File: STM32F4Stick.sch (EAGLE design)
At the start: 42 parts, among them U1 MIC5219 3.3V, U2 USD-SOCKETNEW

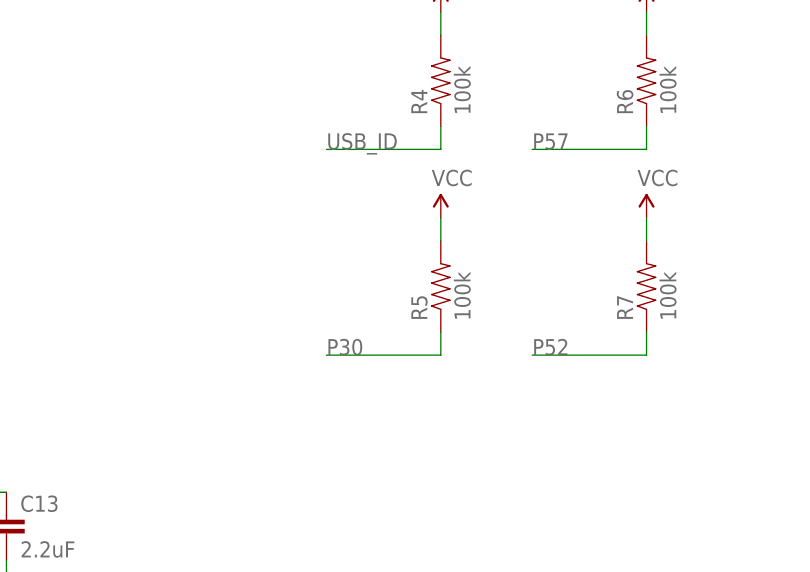
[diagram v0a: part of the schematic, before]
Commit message: Version 1 Rev B. Added STM32F401 support. Added Readme. Added image. Added libraries. Added BOM.
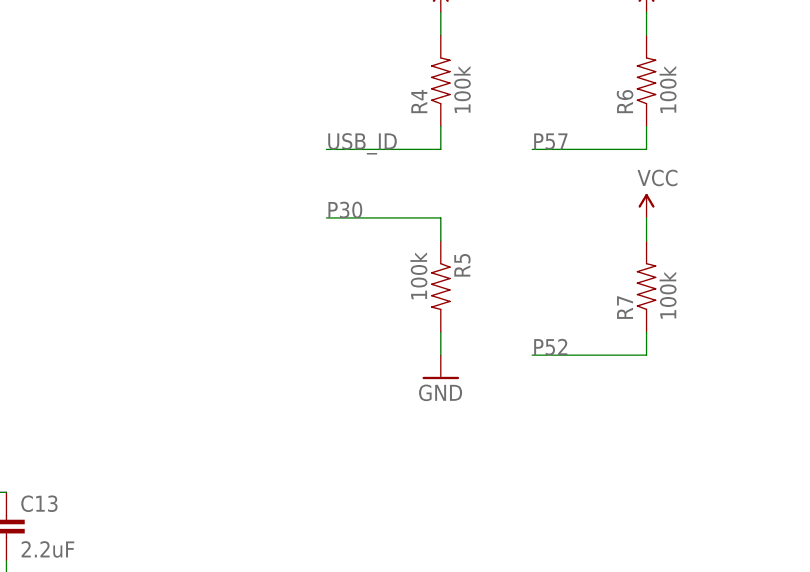
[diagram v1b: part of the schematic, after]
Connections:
- net GND: now also R5.2
- net VCC: no longer R5.2
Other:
- note added: "For STM32F401 support C13 should be 0 ohm resistor"
- note added: "For STM32F401 support C5 should be 0 ohm resistor"
- note added: "For STM32F401 support R5 should be 4.7uF Cap"
- note added: "PA10, PB5, PB11, PC11 needs stable levels for USB bootloader PA10 (USB_ID) is pulled high PB11 (P30) is pulled low PB5 (P57) is pulled high PC11 (P52) is pulled high"
- note removed: "PA10, PB5, PB11, PC11 needs stable levels for USB bootloader PA10 (USB_ID) is pulled high PB11 (P30) is pulled high PB5 (P57) is pulled high PC11 (P52) is pulled high"
- moved on the sheet: R5
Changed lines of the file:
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@@
 <part name="SUPPLY4" library="SparkFun-Aesthetics" deviceset="VCC" device=""/>
 <part name="R5" library="SparkFun-Resistors" deviceset="100KOHM1/10W1%(0603)" device="" value="100k"/>
-<part name="SUPPLY5" library="SparkFun-Aesthetics" deviceset="VCC" device=""/>
 <part name="R7" library="SparkFun-Resistors" deviceset="100KOHM1/10W1%(0603)" device="" value="100k"/>
 <part name="SUPPLY7" library="SparkFun-Aesthetics" deviceset="VCC" device=""/>
@@
 <part name="C15" library="SparkFun-Capacitors" deviceset="0.1UF-25V-5%(0603)" device="" value="0.1uF"/>
 <part name="GND18" library="SparkFun-Aesthetics" deviceset="GND" device=""/>
+<part name="GND19" library="SparkFun-Aesthetics" deviceset="GND" device=""/>
 </parts>
 <sheets>
@@
 levels for USB bootloader
 PA10 (USB_ID) is pulled high
-PB11 (P30) is pulled high
+PB11 (P30) is pulled low
 PB5 (P57) is pulled high
 PC11 (P52) is pulled high</text>
 <text x="22.86" y="203.2" size="1.778" layer="150">External power / USB Power select
 Put a jumper between pins 2-3 for USB power</text>
+<text x="284.48" y="200.66" size="1.778" layer="150">For STM32F401 support
+R5 should be 4.7uF Cap</text>
+<text x="99.06" y="167.64" size="1.778" layer="150">For STM32F401 support
+C5 should be 0 ohm resistor</text>
+<text x="246.38" y="175.26" size="1.778" layer="150">For STM32F401 support
+C13 should be 0 ohm resistor</text>
 </plain>
 <instances>
@@
 <instance part="R4" gate="G$1" x="297.18" y="243.84" rot="R90"/>
 <instance part="SUPPLY4" gate="G$1" x="297.18" y="251.46"/>
-<instance part="R5" gate="G$1" x="297.18" y="220.98" rot="R90"/>
-<instance part="SUPPLY5" gate="G$1" x="297.18" y="228.6"/>
+<instance part="R5" gate="G$1" x="297.18" y="220.98" rot="R270"/>
 <instance part="R7" gate="G$1" x="320.04" y="220.98" rot="R90"/>
 <instance part="SUPPLY7" gate="G$1" x="320.04" y="228.6"/>
@@
 <instance part="C15" gate="G$1" x="63.5" y="142.24"/>
 <instance part="GND18" gate="1" x="63.5" y="132.08"/>
+<instance part="GND19" gate="1" x="297.18" y="210.82"/>
 </instances>
 <busses>
@@
 </segment>
 <segment>
-<pinref part="SUPPLY5" gate="G$1" pin="VCC"/>
-<pinref part="R5" gate="G$1" pin="2"/>
-<wire x1="297.18" y1="228.6" x2="297.18" y2="226.06" width="0.1524" layer="91"/>
-</segment>
-<segment>
 <pinref part="SUPPLY7" gate="G$1" pin="VCC"/>
 <pinref part="R7" gate="G$1" pin="2"/>
@@
 <wire x1="63.5" y1="139.7" x2="63.5" y2="134.62" width="0.1524" layer="91"/>
 </segment>
+<segment>
+<pinref part="R5" gate="G$1" pin="2"/>
+<pinref part="GND19" gate="1" pin="GND"/>
+<wire x1="297.18" y1="215.9" x2="297.18" y2="213.36" width="0.1524" layer="91"/>
+</segment>
 </net>
 <net name="N$10" class="0">
@@
 </segment>
 <segment>
-<wire x1="284.48" y1="213.36" x2="297.18" y2="213.36" width="0.1524" layer="91"/>
-<wire x1="297.18" y1="213.36" x2="297.18" y2="215.9" width="0.1524" layer="91"/>
+<wire x1="284.48" y1="228.6" x2="297.18" y2="228.6" width="0.1524" layer="91"/>
+<wire x1="297.18" y1="228.6" x2="297.18" y2="226.06" width="0.1524" layer="91"/>
 <pinref part="R5" gate="G$1" pin="1"/>
-<label x="284.48" y="213.36" size="1.778" layer="95"/>
-</segment>
-</net>
+<label x="284.48" y="228.6" size="1.778" layer="95"/>
+</segment>
+</net>
